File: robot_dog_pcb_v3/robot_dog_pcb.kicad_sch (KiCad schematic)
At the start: 9 parts, among them J1 Conn_01x02, J2 Conn_01x04, J3 Conn_01x04_Socket/ DIST SENSE, SW1 SW_SPST, U1 ESP32-C3_SUPERMINI_TH, U2 Adafruit-MAX98357-I2S-Amp-Bre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, U3 Adafruit-16-Channel-PWM-Servo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

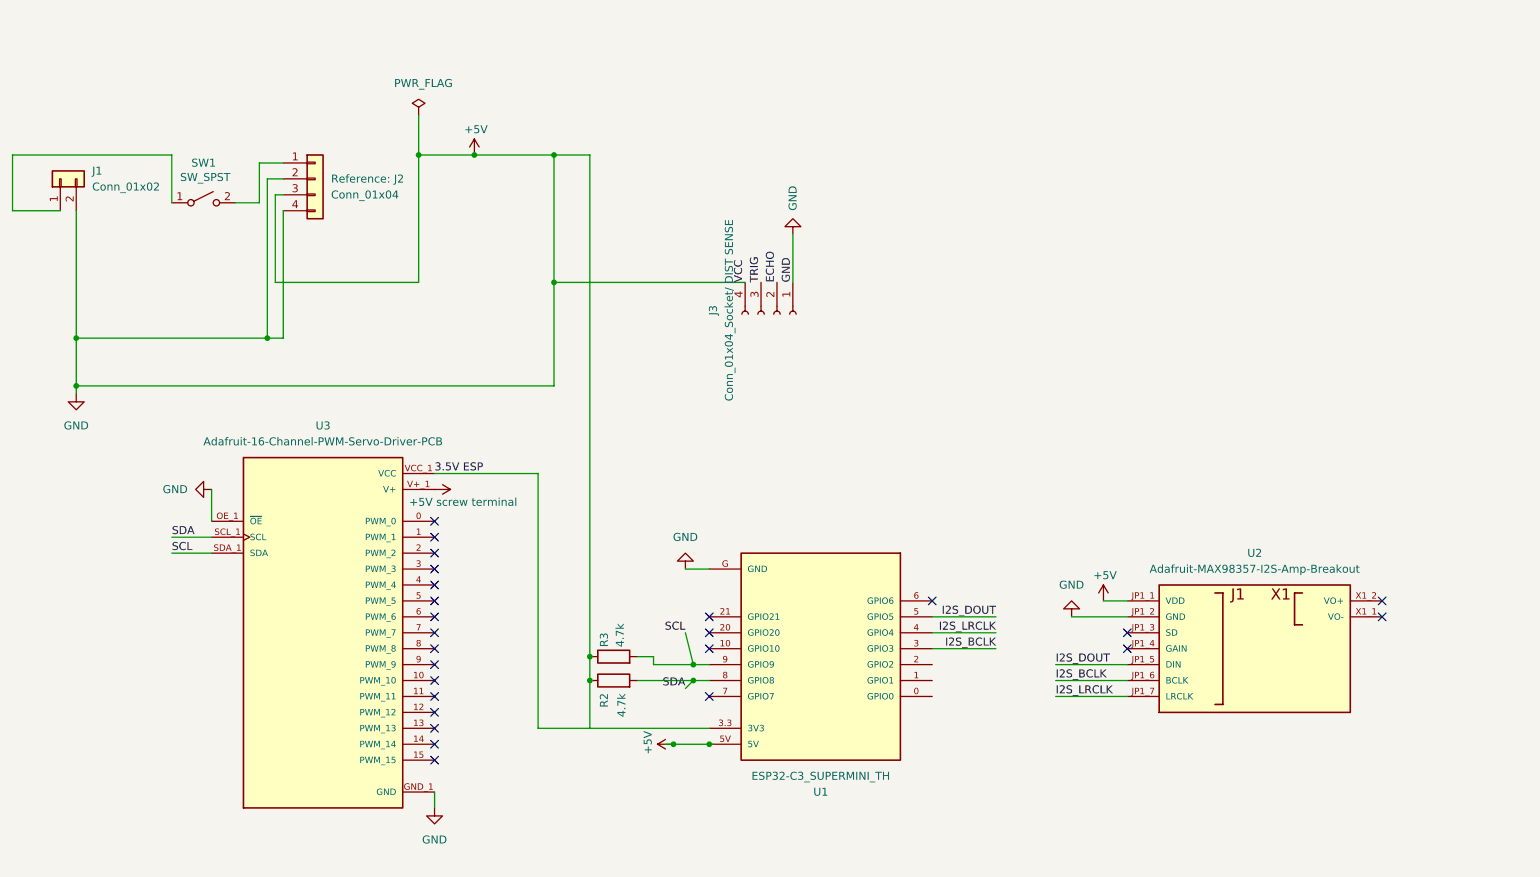
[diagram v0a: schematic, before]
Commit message: design with pin placement, extra pins and traces done
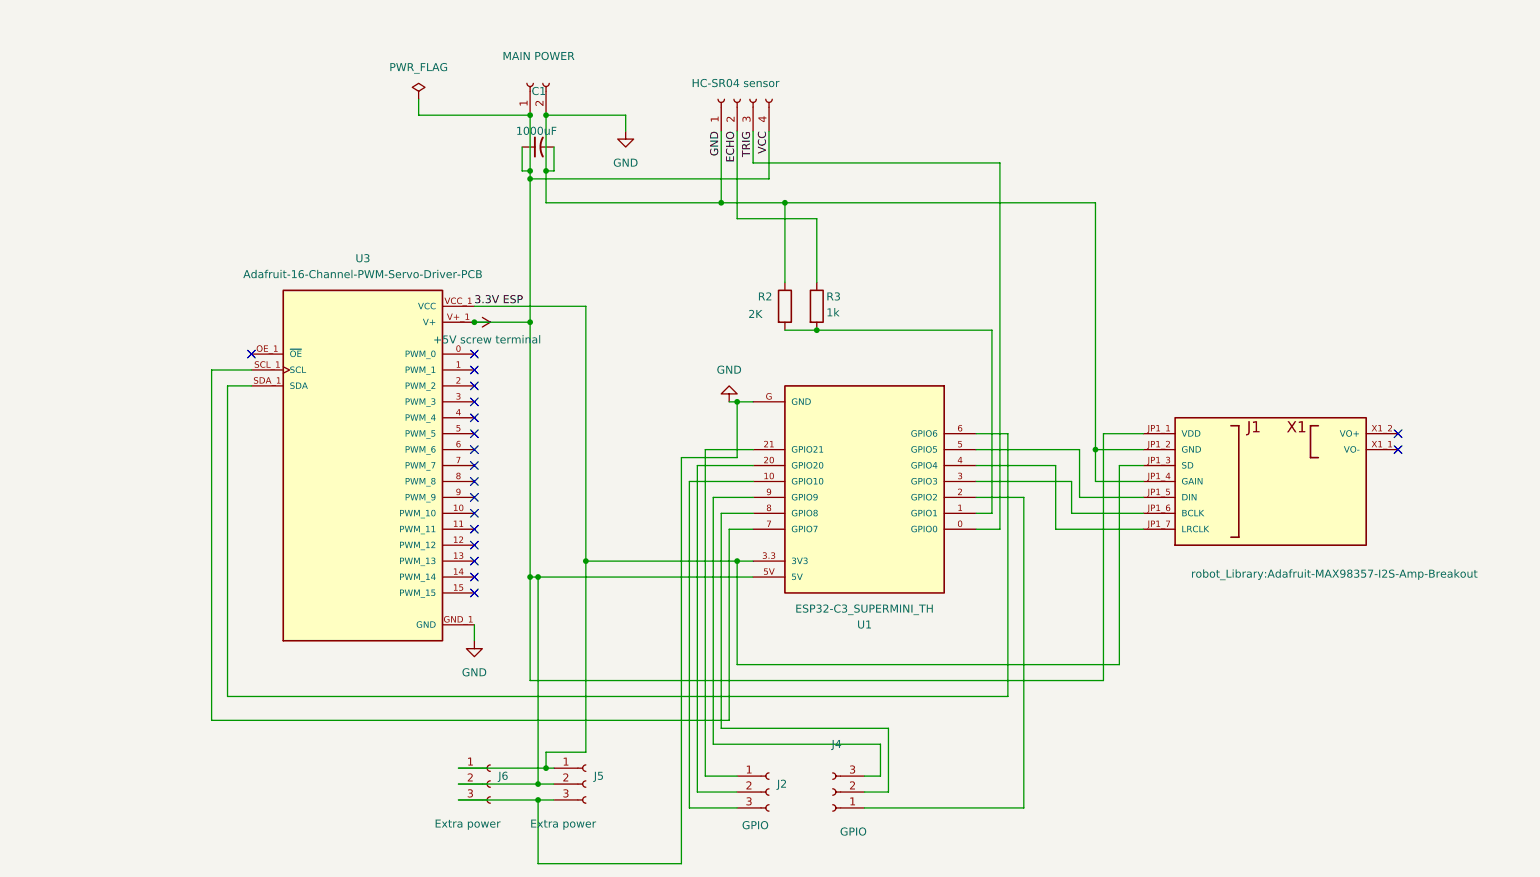
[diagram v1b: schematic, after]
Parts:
- removed J1: Conn_01x02, symbol Connector_Generic:Conn_01x02
- removed J2: Conn_01x04, symbol Connector_Generic:Conn_01x04
- removed SW1: SW_SPST, symbol Switch:SW_SPST
- added C1: 1000uF, Capacitor_THT:C_Radial_D10.0mm_H12.5mm_P5.00mm, symbol Device:C_Small_US
- added J1: MAIN POWER, Connector_AMASS:AMASS_XT30PW-M_1x02_P2.50mm_Horizontal, symbol Connector:Conn_01x02_Socket
- added J2, J4: GPIO, Connector_PinSocket_2.54mm:PinSocket_1x03_P2.54mm_Vertical, symbol Connector:Conn_01x03_Socket
- added J5, J6: Extra power, Connector_PinSocket_2.54mm:PinSocket_1x03_P2.54mm_Vertical, symbol Connector:Conn_01x03_Socket
- J3: value Conn_01x04_Socket/ DIST SENSE -> HC-SR04 sensor; footprint Connector_PinHeader_2.54mm:PinHeader_1x04_P2.54mm_Vertical -> Connector_PinSocket_2.54mm:PinSocket_1x04_P2.54mm_Vertical
- R2: value 4.7k -> 2K; footprint (none) -> Resistor_THT:R_Axial_DIN0207_L6.3mm_D2.5mm_P7.62mm_Horizontal
- R3: value 4.7k -> 1k; footprint (none) -> Resistor_THT:R_Axial_DIN0207_L6.3mm_D2.5mm_P7.62mm_Horizontal
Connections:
- net +5V screw terminal: now also J3.4 (Pin_4), U1.3.3 (3V3), U1.5V, U2.JP1_1 (VDD), U2.JP1_3 (SD), U3.VCC_1 (VCC), U3.VCC_2 (VCC), C1.1, J1.1 (5V_MAIN), J5.1 (Pin_1), J5.2 (Pin_2), J6.1 (Pin_1), J6.2 (Pin_2)
- net ECHO: now also R3.1
- net TRIG: now also U1.0 (GPIO0)
- net GND: now reaches U2.JP1_4 (GAIN)
- net GND: now also J3.1 (GND), R2.1, U1.G (GND), U2.JP1_2 (GND), U3.GND_1 (GND), U3.GND_10 (GND), U3.GND_11 (GND), U3.GND_12 (GND), U3.GND_13 (GND), U3.GND_14 (GND), U3.GND_15 (GND), U3.GND_16 (GND), U3.GND_17 (GND), U3.GND_18 (GND), U3.GND_2 (GND), U3.GND_3 (GND), U3.GND_4 (GND), U3.GND_5 (GND), U3.GND_6 (GND), U3.GND_7 (GND), U3.GND_8 (GND), U3.GND_9 (GND), C1.2, J1.2 (GND_MAIN), J5.3 (Pin_3), J6.3 (Pin_3)
- net at U1.1 (GPIO1): now also R2.2, R3.2
- net at U1.10 (GPIO10): now also J2.3 (Pin_3)
- net at U1.2 (GPIO2): now also J4.1 (Pin_1)
- net at U1.20 (GPIO20): now also J2.2 (Pin_2)
- net at U1.21 (GPIO21): now also J2.1 (Pin_1)
- net at U1.6 (GPIO6): now also U3.SDA_1 (SDA), U3.SDA_2 (SDA)
- net at U1.7 (GPIO7): now also U3.SCL_1 (SCL), U3.SCL_2 (SCL)
- removed net +5V: J3.1 (Pin_1), J3.4 (Pin_4), R2.1, R3.1, U1.3.3 (3V3), U1.5V, U1.G (GND), U2.JP1_1 (VDD), U2.JP1_2 (GND), U3.GND_1 (GND), U3.GND_10 (GND), U3.GND_11 (GND), U3.GND_12 (GND), U3.GND_13 (GND), U3.GND_14 (GND), U3.GND_15 (GND), U3.GND_16 (GND), U3.GND_17 (GND), U3.GND_18 (GND), U3.GND_2 (GND), U3.GND_3 (GND), U3.GND_4 (GND), U3.GND_5 (GND), U3.GND_6 (GND), U3.GND_7 (GND), U3.GND_8 (GND), U3.GND_9 (GND), U3.OE_1 (~{OE}), U3.OE_2 (~{OE}), U3.VCC_1 (VCC), U3.VCC_2 (VCC)
- net I2S_BCLK: no longer names the net of U1.3 (GPIO3), U2.JP1_6 (BCLK)
- net I2S_DOUT: no longer names the net of U1.5 (GPIO5), U2.JP1_5 (DIN)
- net I2S_LRCLK: no longer names the net of U1.4 (GPIO4), U2.JP1_7 (LRCLK)
- removed net SCL: R3.2, U1.9 (GPIO9), U3.SDA_1 (SDA), U3.SDA_2 (SDA)
- removed net SDA: R2.2, U1.8 (GPIO8), U3.SCL_1 (SCL), U3.SCL_2 (SCL)
- new net: U3.OE_1 (~{OE}), U3.OE_2 (~{OE})
- new net: J4.2 (Pin_2), U1.8 (GPIO8)
- new net: J4.3 (Pin_3), U1.9 (GPIO9)
- no-connect marks 25 -> 19
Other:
- moved on the sheet: R2, R3, U1, U3

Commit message: corrected pcb flags and wiring
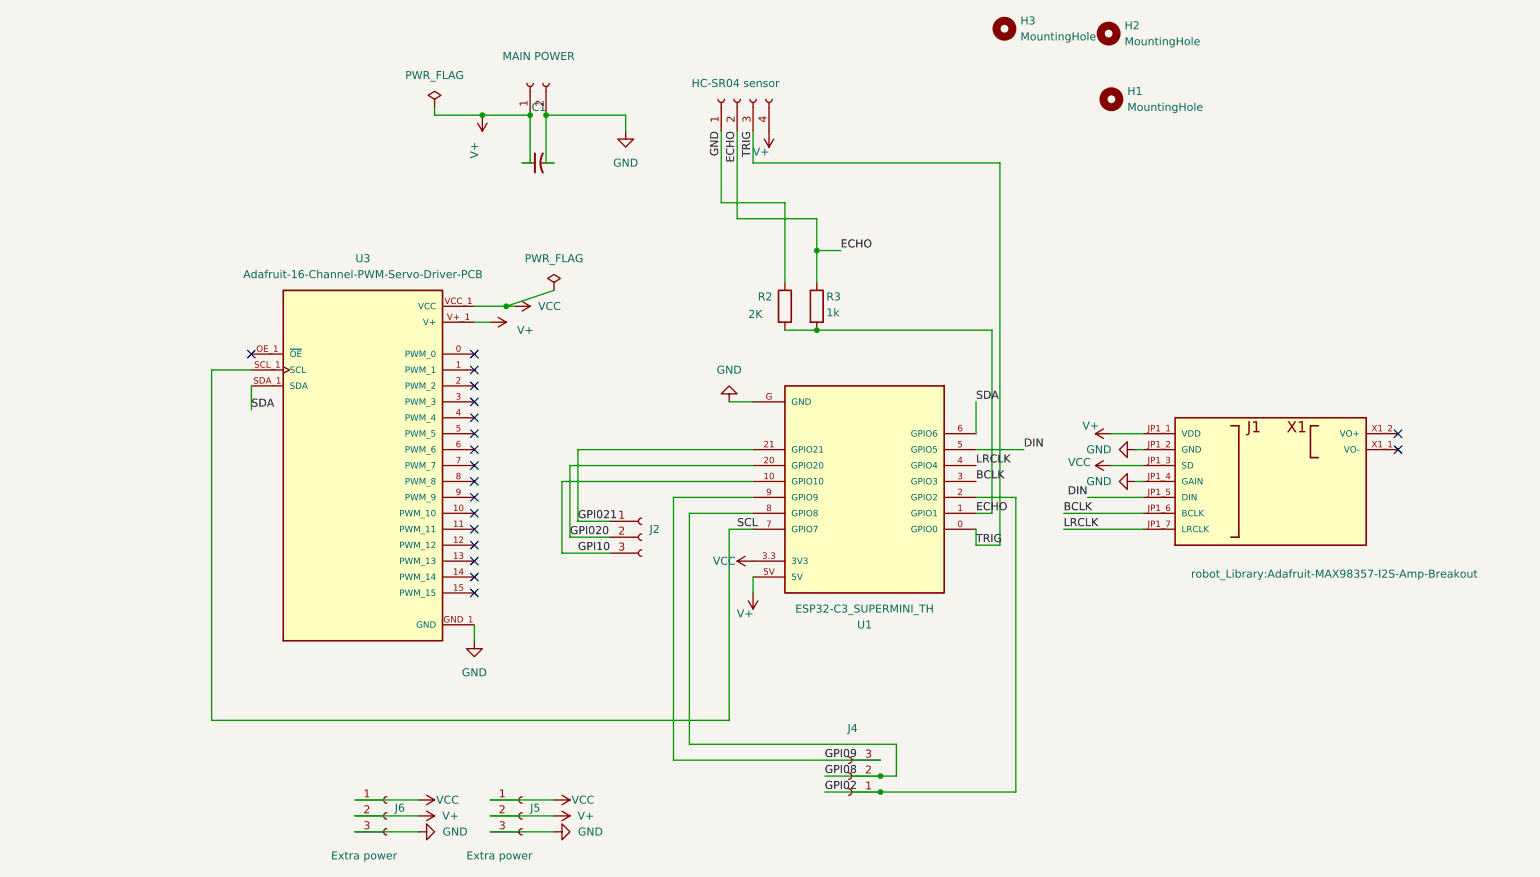
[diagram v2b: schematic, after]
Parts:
- added H1, H2, H3: MountingHole, MountingHole:MountingHole_3mm, symbol Mechanical:MountingHole
- U3: footprint robot_Library:Adafruit-16-Channel-PWM-Servo-Driver-PCB -> robot_Library:PCB ONLY Adafruit-16-Channel-PWM-Servo-Driver-PCB
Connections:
- net ECHO: now also R2.2, R3.2, U1.1 (GPIO1)
- net GPI021: now reaches J2.1 (Pin_1), U1.21 (GPIO21)
- net GPI020: now reaches J2.2 (Pin_2), U1.20 (GPIO20)
- net GPI10: now reaches J2.3 (Pin_3), U1.10 (GPIO10)
- net SCL: now reaches U1.7 (GPIO7), U3.SCL_1 (SCL), U3.SCL_2 (SCL)
- net SDA: now reaches U1.6 (GPIO6), U3.SDA_1 (SDA), U3.SDA_2 (SDA)
- net GPI02: now reaches J4.1 (Pin_1), U1.2 (GPIO2)
- net GPI08: now reaches J4.2 (Pin_2), U1.8 (GPIO8)
- net GPI09: now reaches J4.3 (Pin_3), U1.9 (GPIO9)
- net DIN: now reaches U1.5 (GPIO5), U2.JP1_5 (DIN)
- net BCLK: now reaches U1.3 (GPIO3), U2.JP1_6 (BCLK)
- net LRCLK: now reaches U1.4 (GPIO4), U2.JP1_7 (LRCLK)
- net +5V screw terminal renamed V+
- net V+: no longer J5.1 (Pin_1), J6.1 (Pin_1), U1.3.3 (3V3), U2.JP1_3 (SD), U3.VCC_1 (VCC), U3.VCC_2 (VCC)
- new net VCC: J5.1 (Pin_1), J6.1 (Pin_1), U1.3.3 (3V3), U2.JP1_3 (SD), U3.VCC_1 (VCC), U3.VCC_2 (VCC)
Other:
- moved on the sheet: C1, J2, J4, J5, J6
